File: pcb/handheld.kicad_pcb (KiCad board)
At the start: 2 copper layers, 100 x 96.2 mm, 17 parts, among them J1 Conn_01x15_Pin, J2 Conn_01x15_Pin, J3 Conn_02x13_Odd_Even, J4 Conn_01x06, SW1 SW_Push, SW10 SW_Push, SW11 SW_Push, SW12 SW_Push, SW2 SW_Push, SW3 SW_Push, SW4 SW_Push, SW5 SW_Push, SW6 SW_Push, SW7 SW_Push, SW8 SW_Push, SW9 SW_Push, U2 MCP23017x-x-SS

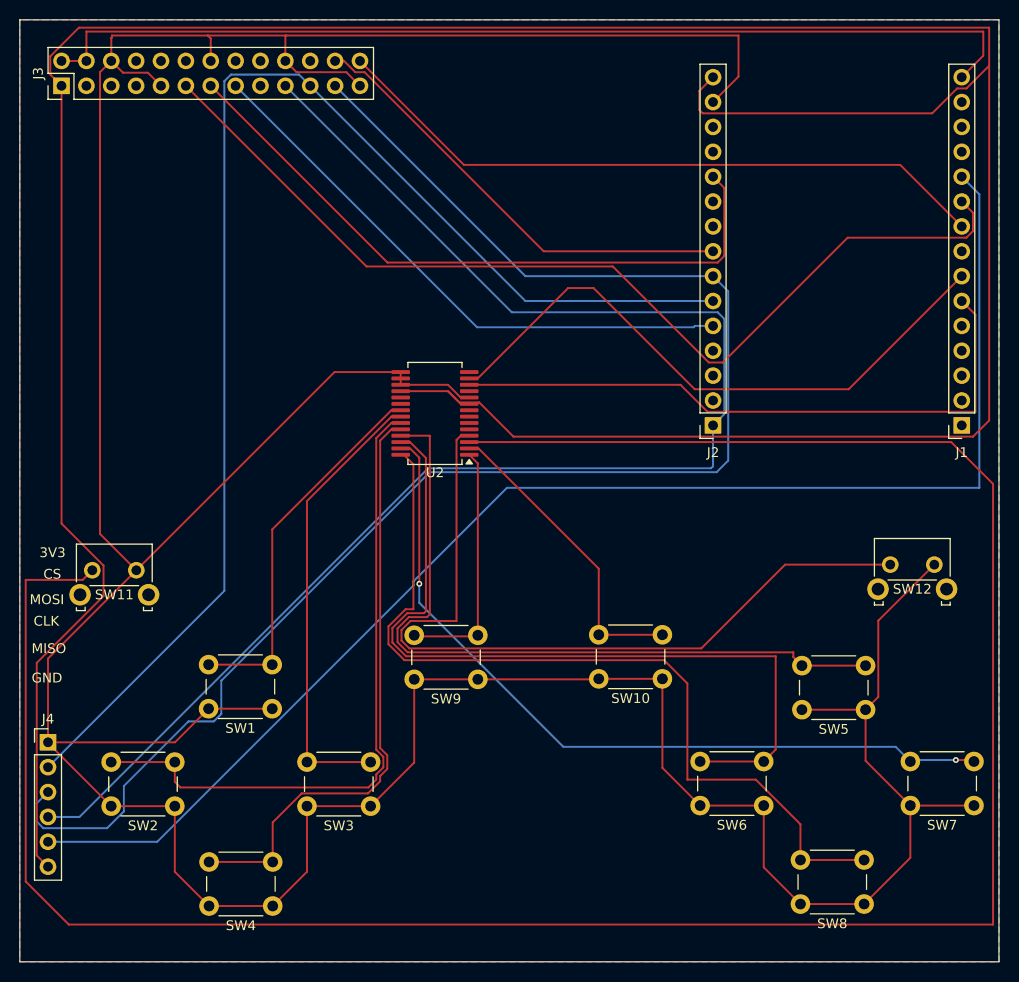
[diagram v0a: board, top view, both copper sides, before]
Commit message: rounded corners
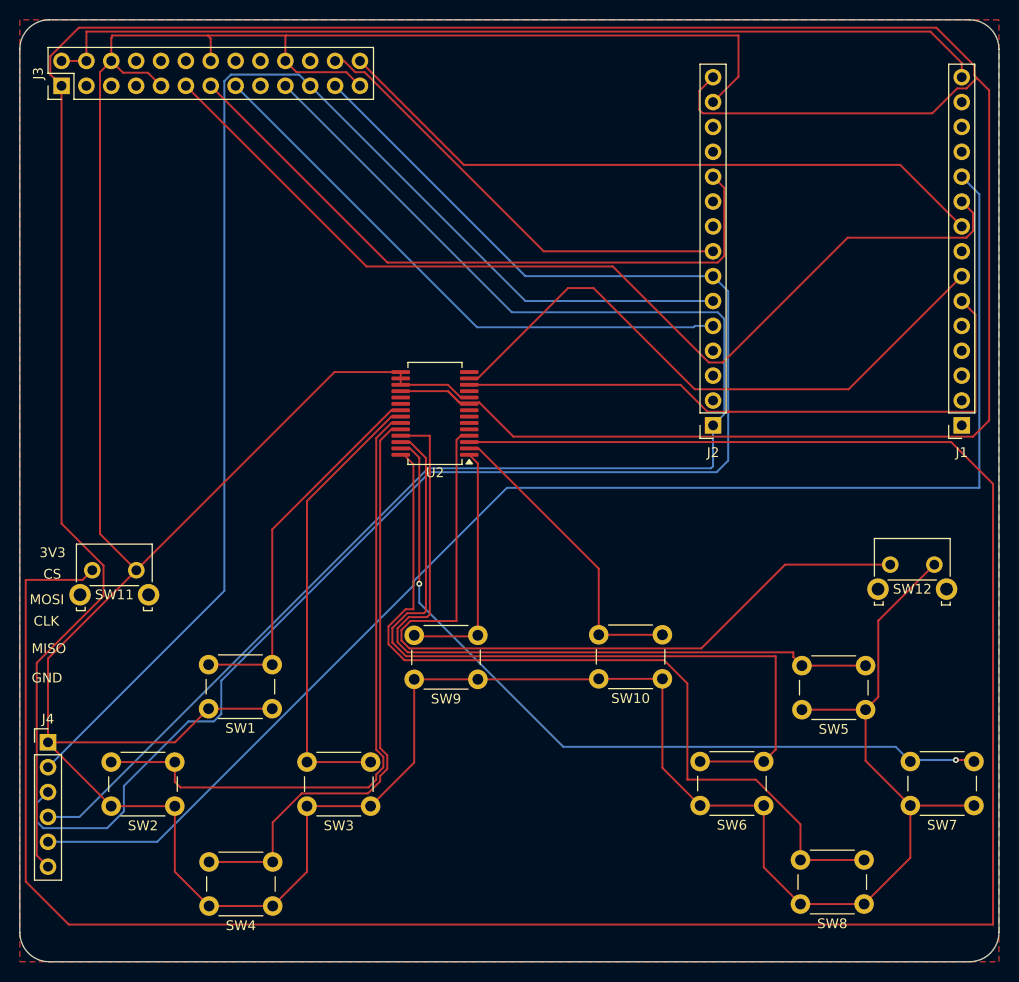
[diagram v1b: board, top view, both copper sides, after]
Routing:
- net +5V: track 102.7 -> 97.7 mm
- net +3V3: track 326.6 -> 321.7 mm
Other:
- outline, holes or cut-outs redrawn
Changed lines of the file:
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@@
 		)
 		(embedded_fonts no)
-		(model "C:/Users/Nmsou/Documents/GitHub/Handheld/Handheld/esp32.step"
+		(model "C:/Users/Nmsou/Documents/GitHub/Handheld/Handheld/3d models/esp32.step"
 			(offset
 				(xyz -12.5 -35 9)
@@
 		)
 		(property "Value" "Conn_01x15_Pin"
-			(at 0 38.33 0)
+			(at 3.2 38.62 0)
 			(layer "F.Fab")
 			(effects
@@
 		)
 		(embedded_fonts no)
-		(model "C:/Users/Nmsou/Documents/GitHub/Handheld/Handheld/screen.wrl"
+		(model "C:/Users/Nmsou/Documents/GitHub/Handheld/Handheld/3d models/screen.wrl"
 			(offset
 				(xyz -23.5 -24.2 10)
@@
 		)
 	)
-	(gr_rect
-		(start 20.2 19.4)
-		(end 120.2 115.6)
+	(gr_arc
+		(start 20.2 22.4)
+		(mid 21.07868 20.27868)
+		(end 23.2 19.4)
+		(stroke
+			(width 0.05)
+			(type default)
+		)
+		(layer "Edge.Cuts")
+	)
+	(gr_line
+		(start 20.2 112.6)
+		(end 20.2 22.4)
+		(stroke
+			(width 0.05)
+			(type default)
+		)
+		(layer "Edge.Cuts")
+	)
+	(gr_line
+		(start 23.2 19.4)
+		(end 117.2 19.4)
+		(stroke
+			(width 0.05)
+			(type default)
+		)
+		(layer "Edge.Cuts")
+	)
+	(gr_arc
+		(start 23.2 115.6)
+		(mid 21.07868 114.72132)
+		(end 20.2 112.6)
+		(stroke
+			(width 0.05)
+			(type default)
+		)
+		(layer "Edge.Cuts")
+	)
+	(gr_arc
+		(start 117.2 19.4)
+		(mid 119.32132 20.27868)
+		(end 120.2 22.4)
+		(stroke
+			(width 0.05)
+			(type default)
+		)
+		(layer "Edge.Cuts")
+	)
+	(gr_line
+		(start 117.2 115.6)
+		(end 23.2 115.6)
+		(stroke
+			(width 0.05)
+			(type default)
+		)
+		(layer "Edge.Cuts")
+	)
+	(gr_line
+		(start 120.2 22.4)
+		(end 120.2 112.6)
+		(stroke
+			(width 0.05)
+			(type default)
+		)
+		(layer "Edge.Cuts")
+	)
+	(gr_arc
+		(start 120.2 112.6)
+		(mid 119.32132 114.72132)
+		(end 117.2 115.6)
 		(stroke
 			(width 0.05)
 			(type default)
 		)
-		(fill no)
 		(layer "Edge.Cuts")
 	)
@@
 	)
 	(segment
+		(start 26.233654 20.2)
+		(end 23.31 23.123654)
+		(width 0.2)
+		(layer "F.Cu")
+		(net "+3V3")
+	)
+	(segment
+		(start 91 25.26)
+		(end 89.6 26.66)
+		(width 0.2)
+		(layer "F.Cu")
+		(net "+3V3")
+	)
+	(segment
 		(start 116.876346 26.41)
-		(end 119.2 24.086346)
+		(end 117.943173 25.343173)
 		(width 0.2)
 		(layer "F.Cu")
@@
 	)
 	(segment
-		(start 117.55 61.97)
-		(end 119.2 60.32)
+		(start 89.95 28.95)
+		(end 113.383654 28.95)
 		(width 0.2)
 		(layer "F.Cu")
@@
 	)
 	(segment
-		(start 119.2 60.32)
-		(end 119.2 24.086346)
+		(start 70.613456 61.97)
+		(end 67.118456 58.475)
 		(width 0.2)
 		(layer "F.Cu")
@@
 	)
 	(segment
-		(start 24.46 26.14)
-		(end 24.46 70.850891)
+		(start 113.383654 28.95)
+		(end 115.923654 26.41)
 		(width 0.2)
 		(layer "F.Cu")
@@
 	)
 	(segment
-		(start 59.1 57.325)
-		(end 63.931544 57.325)
+		(start 23.31 23.123654)
+		(end 23.31 24.99)
 		(width 0.2)
 		(layer "F.Cu")
@@
 	)
 	(segment
-		(start 115.923654 26.41)
-		(end 116.876346 26.41)
+		(start 24.46 26.14)
+		(end 24.46 70.850891)
 		(width 0.2)
 		(layer "F.Cu")
@@
 	)
 	(segment
-		(start 113.383654 28.95)
-		(end 115.923654 26.41)
+		(start 59.1 57.325)
+		(end 63.931544 57.325)
 		(width 0.2)
 		(layer "F.Cu")
@@
 	)
 	(segment
-		(start 23.31 23.123654)
-		(end 23.31 24.99)
+		(start 89.6 26.66)
+		(end 89.6 28.6)
 		(width 0.2)
 		(layer "F.Cu")
@@
 	)
 	(segment
-		(start 63.931544 57.325)
-		(end 65.081544 58.475)
+		(start 119.2 26.6)
+		(end 119.2 60.32)
 		(width 0.2)
 		(layer "F.Cu")
@@
 	)
 	(segment
-		(start 26.233654 20.2)
-		(end 23.31 23.123654)
+		(start 89.6 28.6)
+		(end 89.95 28.95)
 		(width 0.2)
 		(layer "F.Cu")
@@
 	)
 	(segment
-		(start 67.118456 58.475)
-		(end 70.613456 61.97)
+		(start 117.943173 25.343173)
+		(end 119.2 26.6)
 		(width 0.2)
 		(layer "F.Cu")
@@
 	)
 	(segment
+		(start 117.55 61.97)
+		(end 70.613456 61.97)
+		(width 0.2)
+		(layer "F.Cu")
+		(net "+3V3")
+	)
+	(segment
 		(start 63.931544 57.325)
 		(end 65.231544 58.625)
@@
 	)
 	(segment
-		(start 89.95 28.95)
-		(end 113.383654 28.95)
+		(start 65.081544 58.475)
+		(end 63.931544 57.325)
 		(width 0.2)
 		(layer "F.Cu")
@@
 	)
 	(segment
-		(start 89.6 26.66)
-		(end 89.6 28.6)
+		(start 117.686346 25.086346)
+		(end 117.686346 24.086346)
 		(width 0.2)
 		(layer "F.Cu")
@@
 	)
 	(segment
-		(start 89.6 28.6)
-		(end 89.95 28.95)
+		(start 117.943173 25.343173)
+		(end 117.686346 25.086346)
 		(width 0.2)
 		(layer "F.Cu")
@@
 	)
 	(segment
-		(start 65.081544 58.475)
-		(end 67.118456 58.475)
+		(start 119.2 60.32)
+		(end 117.55 61.97)
 		(width 0.2)
 		(layer "F.Cu")
@@
 	)
 	(segment
-		(start 119.2 20.2)
-		(end 26.233654 20.2)
+		(start 115.923654 26.41)
+		(end 116.876346 26.41)
 		(width 0.2)
 		(layer "F.Cu")
@@
 	)
 	(segment
-		(start 91 25.26)
-		(end 89.6 26.66)
+		(start 113.8 20.2)
+		(end 26.233654 20.2)
 		(width 0.2)
 		(layer "F.Cu")
@@
 	)
 	(segment
-		(start 70.613456 61.97)
-		(end 117.55 61.97)
+		(start 117.686346 24.086346)
+		(end 113.8 20.2)
 		(width 0.2)
 		(layer "F.Cu")
@@
 	)
 	(segment
-		(start 119.2 24.086346)
-		(end 119.2 20.2)
+		(start 67.118456 58.475)
+		(end 65.081544 58.475)
 		(width 0.2)
 		(layer "F.Cu")
@@
 	)
 	(segment
-		(start 27 20.6)
-		(end 118.6 20.6)
+		(start 116.4 23.8)
+		(end 116.4 25.26)
 		(width 0.2)
 		(layer "F.Cu")
@@
 	)
 	(segment
-		(start 27 23.6)
-		(end 24.46 23.6)
+		(start 27 20.6)
+		(end 113.2 20.6)
 		(width 0.2)
 		(layer "F.Cu")
@@
 	(segment
 		(start 27 23.6)
-		(end 27 20.6)
+		(end 24.46 23.6)
 		(width 0.2)
 		(layer "F.Cu")
@@
 	)
 	(segment
-		(start 118.6 23.06)
-		(end 116.4 25.26)
+		(start 113.2 20.6)
+		(end 116.4 23.8)
 		(width 0.2)
 		(layer "F.Cu")
@@
 	)
 	(segment
-		(start 118.6 20.6)
-		(end 118.6 23.06)
+		(start 27 23.6)
+		(end 27 20.6)
 		(width 0.2)
 		(layer "F.Cu")
